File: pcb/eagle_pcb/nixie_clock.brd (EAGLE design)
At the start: 130 x 102 mm, 157 parts, among them J1 USB-C-VVERTICAL, J2 8, J3 8, J4 4, J5 4, J6 PH-2, Q1 IRLR3110ZPBF, Q2 BC817-25, Q3 BC817-25, Q4 BC817-25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

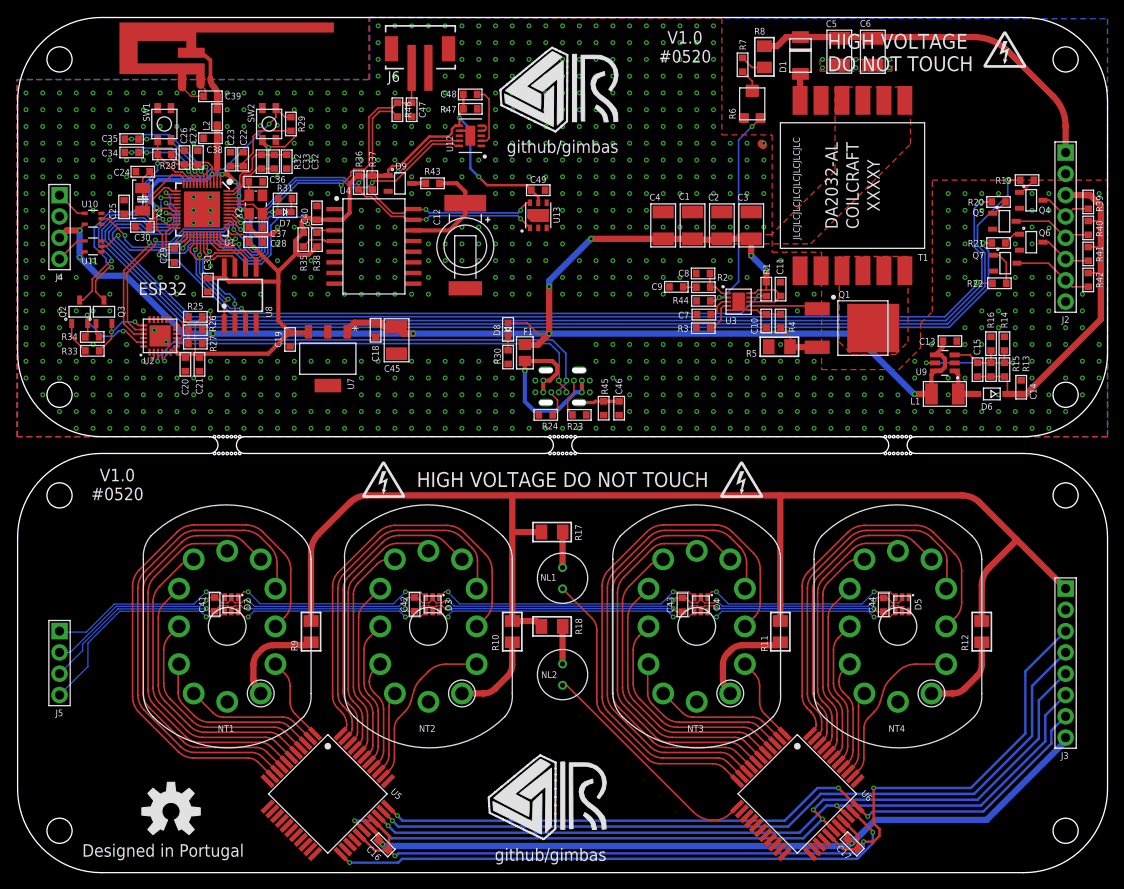
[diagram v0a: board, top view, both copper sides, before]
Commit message: added buzzer
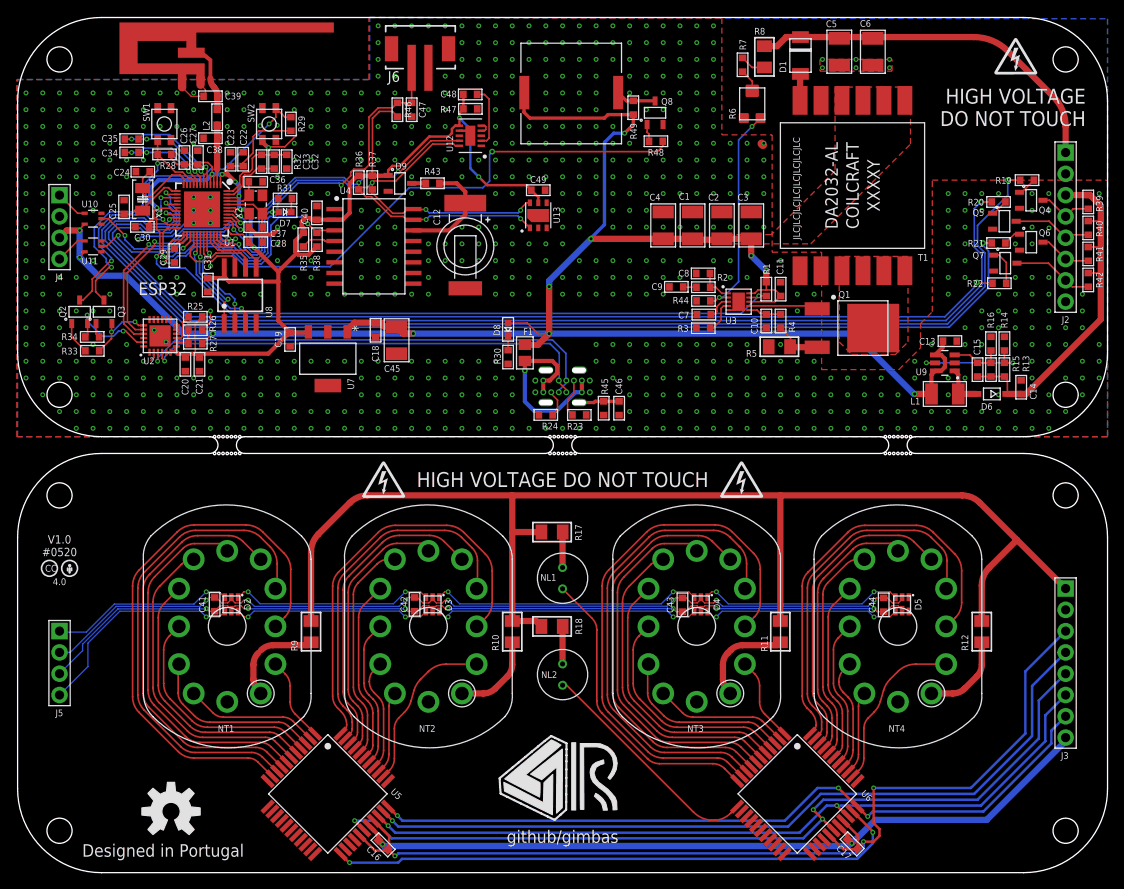
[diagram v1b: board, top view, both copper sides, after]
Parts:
- removed U$2: (no value), Utility > Silkscreen:RAFAEL_SILVA_10MM_ALT
- added B1: (no value), Eletromechanical > Buzzer:BUZZ_PIEZO_SMD
- added Q8: BC817-25, Semiconductors > Discrete Semiconductors > Transistors > Bipolar Transistors - BJT:SOT-23-3
- added R48, R49: 1k, Passive Components > Resistors > Chip Resistors:0603_WAVE
- moved LOGO7 8.49 mm to (121.2, 82.7)
- moved U$1 2.64 mm to (57.5, 6.30)
- moved LOGO6 1.53 mm to (116.5, 95.2)
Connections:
- new net BUZZER: R48.P$2, U1.25
- new net N$38: B1.2, Q8.P$3, R49.P$2
- new net N$39: Q8.P$1, R48.P$1
- net 5V: now also B1.1, R49.P$1
- net GND: now also Q8.P$2
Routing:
- net BUZZER: track 0.00 -> 74.8 mm, vias 0 -> 2
- net 5V: track 192.5 -> 226.0 mm, vias 10 -> 11
- net GND: track 26.7 -> 34.1 mm, vias 785 -> 773
- net N$38: track 0.00 -> 4.81 mm
- net N$39: track 0.00 -> 2.09 mm
- net !HVEN: track 86.9 -> 87.7 mm
- net RTC_INT: track 31.6 -> 32.1 mm
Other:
- board text added: "4.0"
- board text added: "CC"
